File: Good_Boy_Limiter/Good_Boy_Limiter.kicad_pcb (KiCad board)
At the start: 2 copper layers, 76 parts, among them J2 Extra General Pins, Q2 AO3422, SW3 RESET1, SW4 BOOT1, U1 ESP32-S3-WROOM-1, U10 B3B-XH-A, U11 B3B-XH-A, U12 B3B-XH-A, U2 TC4427EOA_C636891, U3 LM2576HVR-12, U4 LM2576SX-3.3/NOPB, U5 SY8120B, U6 AMS1117-3.3, U7 MAX40200AUK+T, U8 B3B-XH-A, U9 LM393DR2G

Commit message: Routing update
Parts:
- added R19: 22, Resistor_SMD:R_0402_1005Metric, F.Cu at (207.8, 52.6)
- added R20: 22, Resistor_SMD:R_0402_1005Metric, F.Cu at (207.8, 53.8)
- U4: value LM2576SX-3.3/NOPB -> USBLC6-2SC6; footprint easyeda2kicad:TO-263-5_L10.2-W8.9-P1.70-TL -> Package_TO_SOT_SMD:SOT-23-6
- moved R2 196.9 mm to (236.7, 113.2), turned to 180 degrees
- moved R1 196.6 mm to (236.7, 110.1), turned to 180 degrees
- moved C1 192.0 mm to (231.4, 39.0)
- moved D3 175.5 mm to (236.6, 61.1), turned to 180 degrees
- moved SW3 168.6 mm to (244.8, 44.2), turned to -90 degrees
- moved U4 162.0 mm to (188.0, 48.8), turned to 90 degrees
- moved SW4 133.4 mm to (244.8, 51.9), turned to -90 degrees
- moved J2 123.7 mm to (233.7, 130.8), turned to 90 degrees
- moved U1 123.6 mm to (220.1, 42.9)
- moved C2 121.1 mm to (81.3, 74.9)
- moved C6 119.9 mm to (231.6, 54.1)
- moved U8 115.5 mm to (243.8, 109.9), turned to -90 degrees
- moved R13 108.3 mm to (99.1, 83.8)
- moved R14 108.3 mm to (99.1, 89.1)
- moved Cin1 96.8 mm to (54.6, 67.3)
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- renumbered U12 to U10, U10 to U12
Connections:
- R15 pad 1: /Voltage Sensing Modules/V_Sensing -> /Voltage Sensing Modules/V_Sensing3
- R17 pad 1: /Voltage Sensing Modules/V_Sensing -> /Voltage Sensing Modules/V_Sensing4
- R2 pad 1: /Voltage Sensing Modules/V_Sensing -> /Voltage Sensing Modules/V_Sensing1
- R4 pad 1: /Voltage Sensing Modules/V_Sensing -> /Voltage Sensing Modules/V_Sensing2
- U1 pad 13: /D- -> Net-(U1-USB_D-)
- U1 pad 14: /D+ -> Net-(U1-USB_D+)
- U10 pad 3: /Voltage Sensing Modules/V_Sensing -> /Voltage Sensing Modules/V_Sensing2
- U11 pad 3: /Voltage Sensing Modules/V_Sensing -> /Voltage Sensing Modules/V_Sensing3
- U12 pad 3: /Voltage Sensing Modules/V_Sensing -> /Voltage Sensing Modules/V_Sensing4
- U4 pad 1: /+12V -> /D+
- U4 pad 2: Net-(D3-K) -> GND
- U4 pad 3: GND -> /D-
- U4 pad 4: /3V3Buck -> /D-
- U4 pad 5: GND -> /5VUSB
- U4 pad 6: GND -> /D+
- U8 pad 3: /Voltage Sensing Modules/V_Sensing -> /Voltage Sensing Modules/V_Sensing1
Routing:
- net /GPIO1: track 0.00 -> 86.6 mm, vias 0 -> 2
- net GND: track 0.00 -> 71.8 mm, vias 0 -> 2
- net /GPIO4: track 0.00 -> 71.5 mm, vias 0 -> 2
- net /GPIO3: track 0.00 -> 39.8 mm
- net /GPIO2: track 0.00 -> 32.9 mm
- net /D-: track 0.00 -> 31.4 mm
- net Net-(D2-K): track 0.00 -> 30.7 mm
- net /D+: track 0.00 -> 30.3 mm
- net /+12V: track 0.00 -> 26.4 mm
- net +48VIN: track 0.00 -> 15.5 mm
- net Net-(Q2-D): track 0.00 -> 13.7 mm
- net Net-(U1-EN): track 15.7 -> 7.85 mm
- net /Voltage Sensing Modules/V_Sensing4: track 0.00 -> 7.47 mm
- net /5VUSB: track 0.00 -> 7.07 mm
- net /Voltage Sensing Modules/V_Sensing2: track 0.00 -> 6.87 mm
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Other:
- board text added: "BOOT"
- board text added: "RESET"

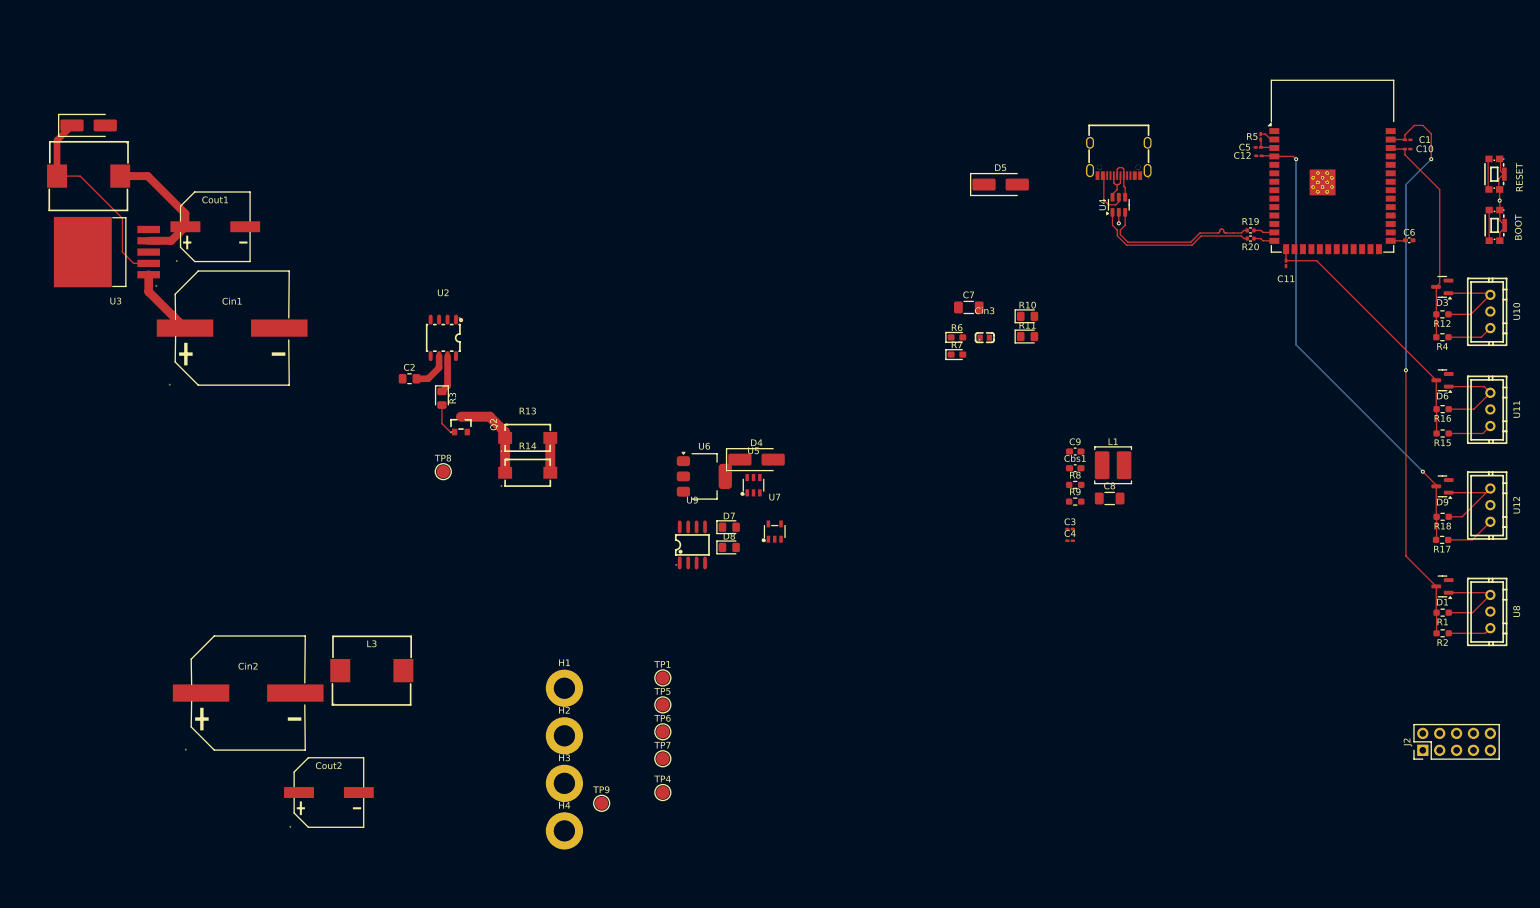
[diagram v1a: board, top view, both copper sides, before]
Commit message: Updated routing
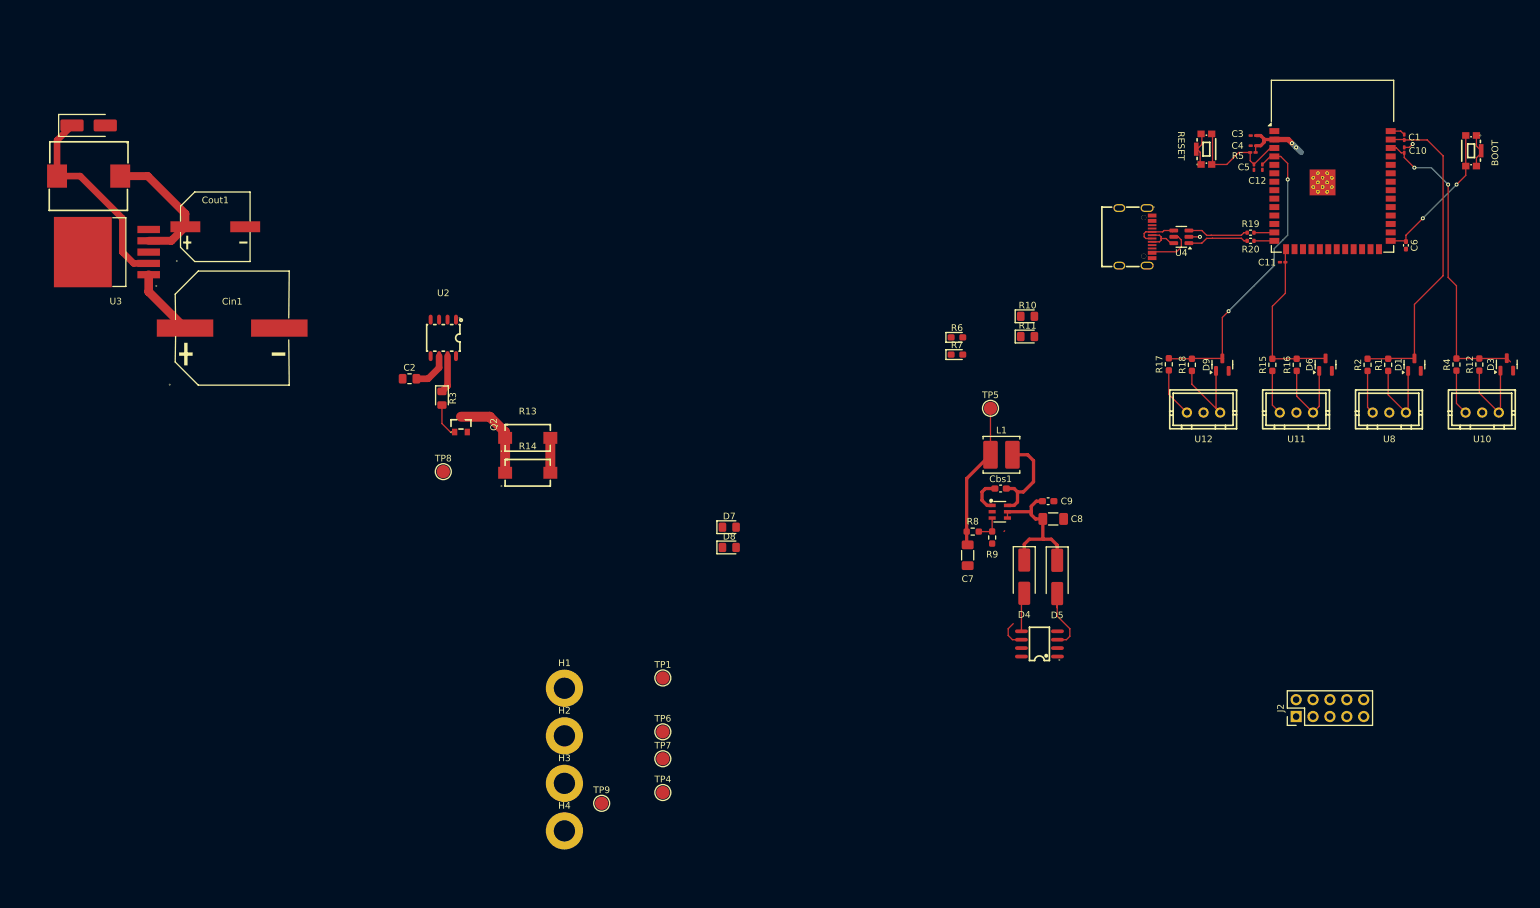
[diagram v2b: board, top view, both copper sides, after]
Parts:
- removed Cin2: 100uF, easyeda2kicad:CAP-SMD_BD16.0-L17.0-W17.0-FD
- removed Cin3: 10uF, easyeda2kicad:C0603
- removed Cout2: 1000uF, easyeda2kicad:CAP-SMD_BD10.0-L10.3-W10.3-FD
- removed L3: SL1050-101M, easyeda2kicad:IND-SMD_L11.5-W10.5
- removed U6: AMS1117-3.3, Package_TO_SOT_SMD:SOT-223-3_TabPin2
- removed U7: MAX40200AUK+T, easyeda2kicad:TSOT-23-5_L2.9-W1.6-P0.95-LS2.8-BL
- moved TP5 66.5 mm to (168.7, 79.4)
- moved C4 65.5 mm to (208.2, 39.9), turned to 180 degrees
- moved C3 65.3 mm to (208.2, 38.4), turned to 180 degrees
- moved D5 59.6 mm to (178.7, 104.7), turned to -90 degrees
- moved U9 54.3 mm to (176.0, 114.8), turned to 90 degrees
- moved R17 48.9 mm to (195.5, 72.8), turned to 90 degrees
- moved U12 45.3 mm to (200.7, 80.0), turned to 180 degrees
- moved SW3 44.2 mm to (200.8, 40.4), turned to 90 degrees
- moved R18 44.1 mm to (198.9, 72.8), turned to 90 degrees
- moved D4 43.9 mm to (173.7, 104.7), turned to -90 degrees
- moved R2 41.9 mm to (225.4, 72.8), turned to 90 degrees
- moved R1 38.2 mm to (228.5, 72.8), turned to 90 degrees
- moved D9 37.8 mm to (203.5, 72.8), turned to 90 degrees
- moved C7 37.3 mm to (165.2, 101.5), turned to -90 degrees
- moved U5 37.3 mm to (170.1, 94.9), turned to -90 degrees
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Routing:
- net /GPIO1: track 86.6 -> 48.3 mm, vias 2 -> 0
- net /3V3: track 2.41 -> 33.7 mm, vias 0 -> 2
- net /GPIO4: track 71.5 -> 46.7 mm
- net /3V3 Selector/Vin: track 0.00 -> 23.3 mm
- net /+12V: track 26.4 -> 42.1 mm
- net /D+: track 30.3 -> 14.8 mm
- net /D-: track 31.4 -> 16.0 mm
- net /GPIO0: track 6.87 -> 22.1 mm, vias 0 -> 2
- net Net-(U5-LX): track 0.00 -> 14.9 mm
- net /GPIO3: track 39.8 -> 25.4 mm
- net /GPIO2: track 32.9 -> 46.6 mm, vias 0 -> 2
- net Net-(U1-EN): track 7.85 -> 17.4 mm
- net /5VUSB: track 7.07 -> 13.0 mm
- net Net-(U5-BS): track 0.00 -> 5.25 mm
- net Net-(U5-FB): track 0.00 -> 4.18 mm

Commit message: More update on routing
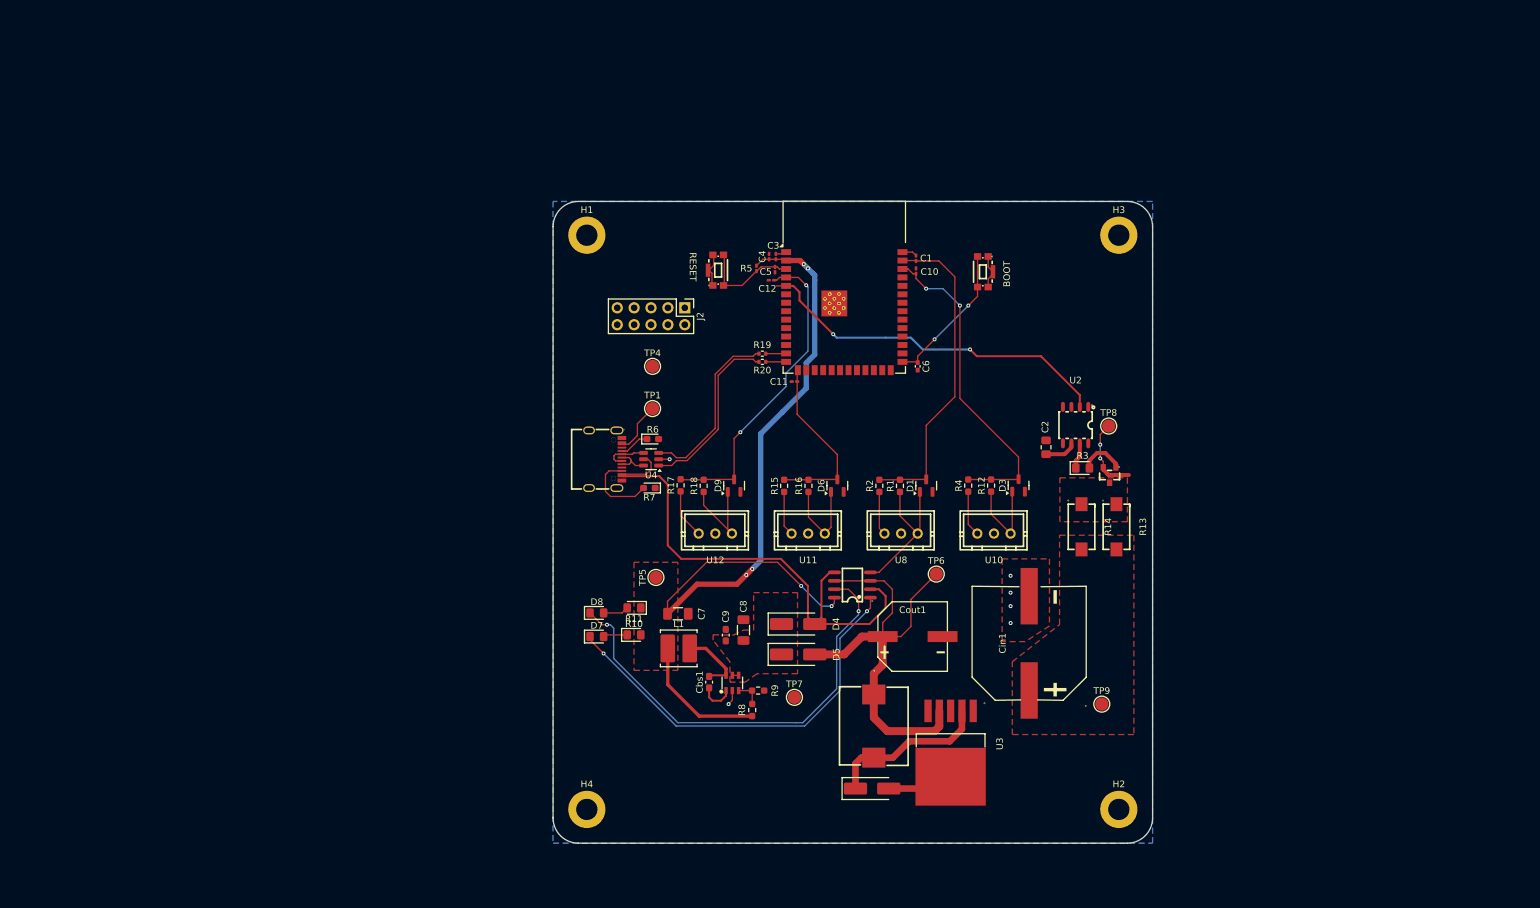
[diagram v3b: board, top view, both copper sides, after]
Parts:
- moved D2 154.4 mm to (150.9, 136.6)
- moved U3 145.7 mm to (162.7, 129.8), turned to -90 degrees
- moved L2 144.2 mm to (151.1, 127.2), turned to -90 degrees
- moved Cin1 128.9 mm to (174.5, 114.7), turned to 90 degrees
- moved Cout1 121.6 mm to (156.9, 113.7)
- moved H3 117.3 mm to (188.0, 53.3)
- moved J2 110.6 mm to (122.7, 64.3), turned to -90 degrees
- moved TP8 100.3 mm to (186.4, 82.0)
- moved Q2 97.8 mm to (186.6, 89.4), turned to 90 degrees
- moved R3 96.9 mm to (182.5, 88.4), turned to 0 degrees
- moved C2 96.3 mm to (177.0, 85.2), turned to -90 degrees
- moved U2 96.0 mm to (181.5, 81.9)
- moved R13 89.5 mm to (187.6, 97.2), turned to -90 degrees
- moved U4 86.5 mm to (117.6, 87.0)
- moved USB1 86.5 mm to (110.8, 87.0)
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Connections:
- net Net-(Q2-D) renamed /Drain
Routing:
- net /3V3: track 33.7 -> 128.1 mm, vias 2 -> 6
- net /5VUSB: track 13.0 -> 86.8 mm
- net Net-(D8-K): track 0.00 -> 67.8 mm, vias 0 -> 2
- net Net-(D7-K): track 0.00 -> 61.6 mm, vias 0 -> 2
- net /GPIO5: track 0.00 -> 55.0 mm, vias 0 -> 2
- net /+12V: track 42.1 -> 73.5 mm
- net /3V3 Selector/Vin: track 23.3 -> 0.95 mm
- net GND: track 72.2 -> 94.2 mm
- net /D+: track 14.8 -> 32.2 mm
- net /D-: track 16.0 -> 33.3 mm
- net +48VIN: track 15.5 -> 0.00 mm
- net /Drain: track 13.7 -> 0.04 mm
- net Net-(USB1-CC2): track 0.00 -> 11.8 mm
- net +48VOUT: track 0.00 -> 11.5 mm, vias 0 -> 2
- net Net-(D2-K): track 30.7 -> 24.7 mm
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- added copper zone on F.Cu, net +48VIN
- added copper zone on F.Cu, net /3V3
- added copper zone on F.Cu, net /3V3 Selector/Vin
- added copper zone on F.Cu, net /Drain
- added copper zone on B.Cu, net GND
- added copper zone on F.Cu, net GND
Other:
- board outline added: 90.2 x 96.5 mm

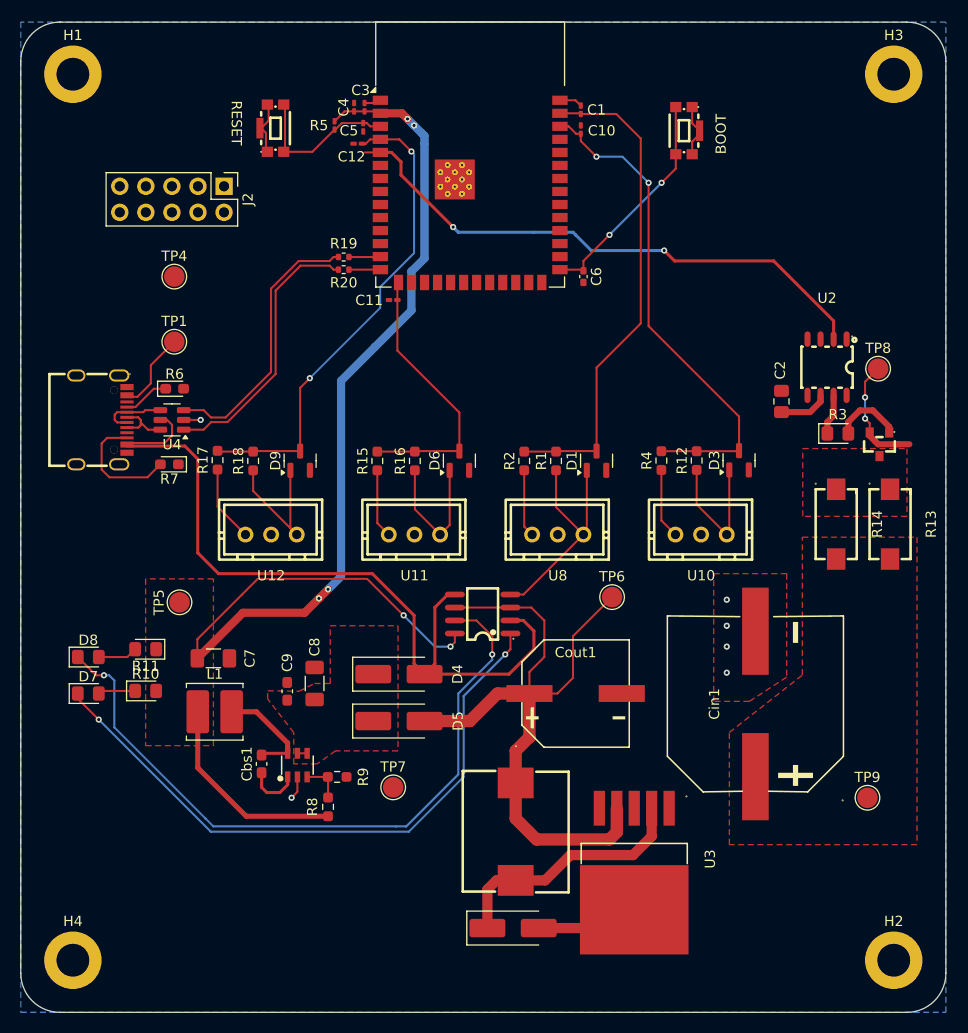
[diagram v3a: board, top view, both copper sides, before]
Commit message: Added xt30 adn routed, ready for revision
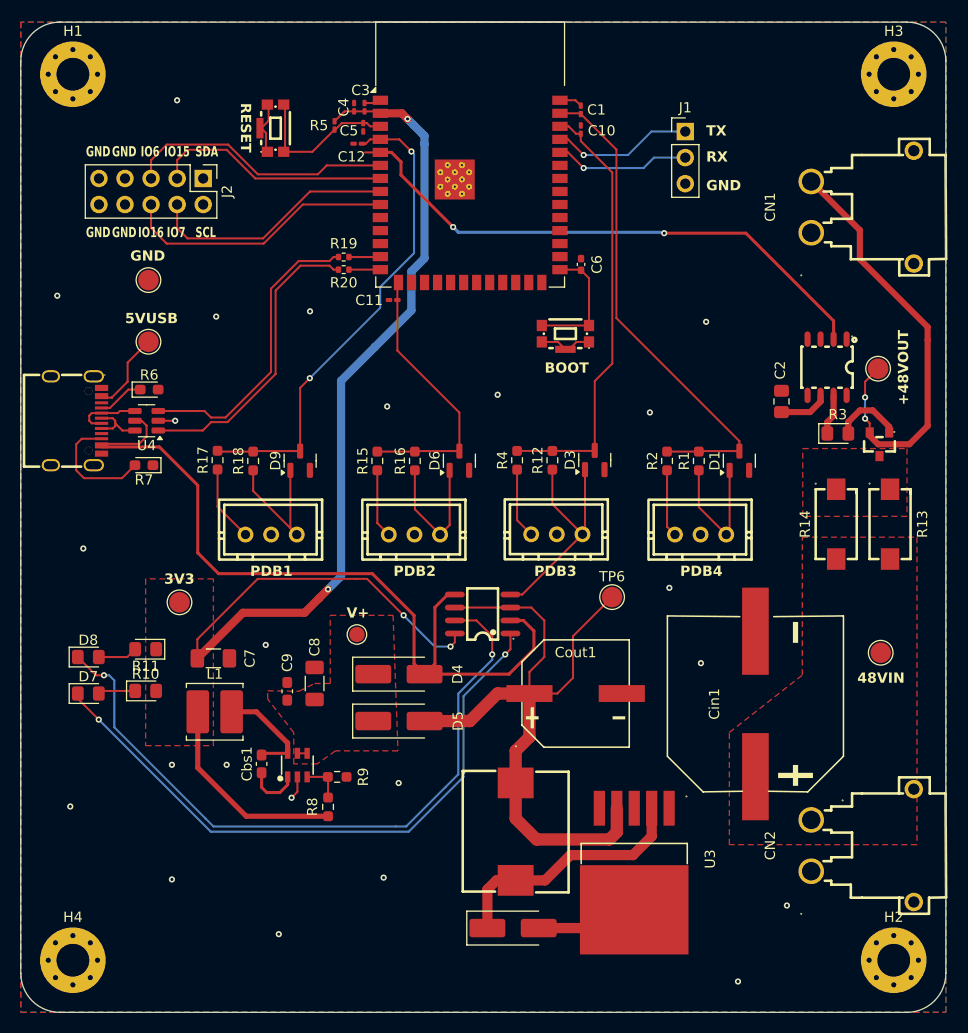
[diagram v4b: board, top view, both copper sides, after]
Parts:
- added CN1: XT30PW-M, easyeda2kicad:CONN-TH_XT30PW-M, F.Cu at (184.9, 66.3)
- added CN2: XT30PW-M, easyeda2kicad:CONN-TH_XT30PW-M, F.Cu at (184.9, 128.5)
- added J1: UART, Connector_PinHeader_2.54mm:PinHeader_1x03_P2.54mm_Vertical, F.Cu at (167.6, 58.9)
- H1, H2, H3, H4: footprint MountingHole:MountingHole_3.2mm_M3_DIN965_Pad -> MountingHole:MountingHole_3.2mm_M3_Pad_Via
- TP7: footprint TestPoint:TestPoint_Pad_D2.0mm -> TestPoint:TestPoint_Pad_D1.5mm
- moved SW4 23.4 mm to (156.0, 79.0), turned to 180 degrees
- moved TP7 15.3 mm to (135.6, 108.0)
- moved TP9 14.2 mm to (186.7, 109.7)
- moved D3 14.1 mm to (158.8, 90.9)
- moved R12 14.1 mm to (154.7, 91.0)
- moved R4 14.1 mm to (151.2, 91.0)
- moved U10 14.1 mm to (155.1, 98.2)
- moved D1 13.9 mm to (172.9, 91.0)
- moved U8 13.9 mm to (169.1, 98.2)
- moved R1 13.9 mm to (169.0, 91.0)
- moved R2 13.9 mm to (165.9, 91.0)
- moved TP4 2.54 mm to (115.3, 73.4)
- moved TP1 2.52 mm to (115.3, 79.4)
- moved R6 2.48 mm to (115.4, 84.1)
- moved R7 2.48 mm to (114.9, 91.4)
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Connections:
- J2 pad 1: /TX -> /SDA
- J2 pad 10: /GPIO6 -> GND
- J2 pad 2: /RX -> /SCL
- J2 pad 3: /SDA -> /GPIO7
- J2 pad 4: /SCL -> /GPIO15
- J2 pad 5: GND -> /GPIO6
- J2 pad 6: GND -> /GPIO16
- J2 pad 7: /GPIO16 -> GND
- J2 pad 8: /GPIO15 -> GND
- J2 pad 9: /GPIO7 -> GND
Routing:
- net +48VOUT: track 11.5 -> 42.5 mm
- net /GPIO16: track 0.00 -> 26.8 mm
- net /GPIO6: track 0.00 -> 26.3 mm
- net /GPIO15: track 0.00 -> 24.4 mm
- net /GPIO7: track 0.00 -> 23.2 mm
- net /TX: track 0.00 -> 13.8 mm, vias 0 -> 1
- net /RX: track 0.00 -> 13.3 mm, vias 0 -> 1
- net /GPIO0: track 22.1 -> 12.8 mm, vias 2 -> 0
- net /GPIO2: track 48.9 -> 43.0 mm, vias 2 -> 0
- net /D+: track 32.2 -> 34.7 mm
- net /D-: track 33.3 -> 35.8 mm
- net /5VUSB: track 86.8 -> 87.8 mm
- net GND: track 94.2 -> 94.1 mm, vias 2 -> 23
- net /3V3: vias 6 -> 4
- net (no net): vias 4 -> 0
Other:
- board text added: "+48VOUT"
- board text added: "3V3"
- board text added: "48VIN"
- board text added: "5VUSB"
- board text added: "GND"
- board text added: "IO15"
- board text added: "IO16"
- board text added: "IO6"
- board text added: "IO7"
- board text added: "PDB1"
- board text added: "PDB2"
- board text added: "PDB3"
- board text added: "PDB4"
- board text added: "RX"
- board text added: "SCL"
- board text added: "SDA"
- board text added: "TX"
- board text added: "V+"
